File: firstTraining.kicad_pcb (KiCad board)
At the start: 2 copper layers, 147.3 x 50.8 mm, 17 parts, among them T1 Transformer_1P_SS, U1 TA48M05F, U2 TA48033S

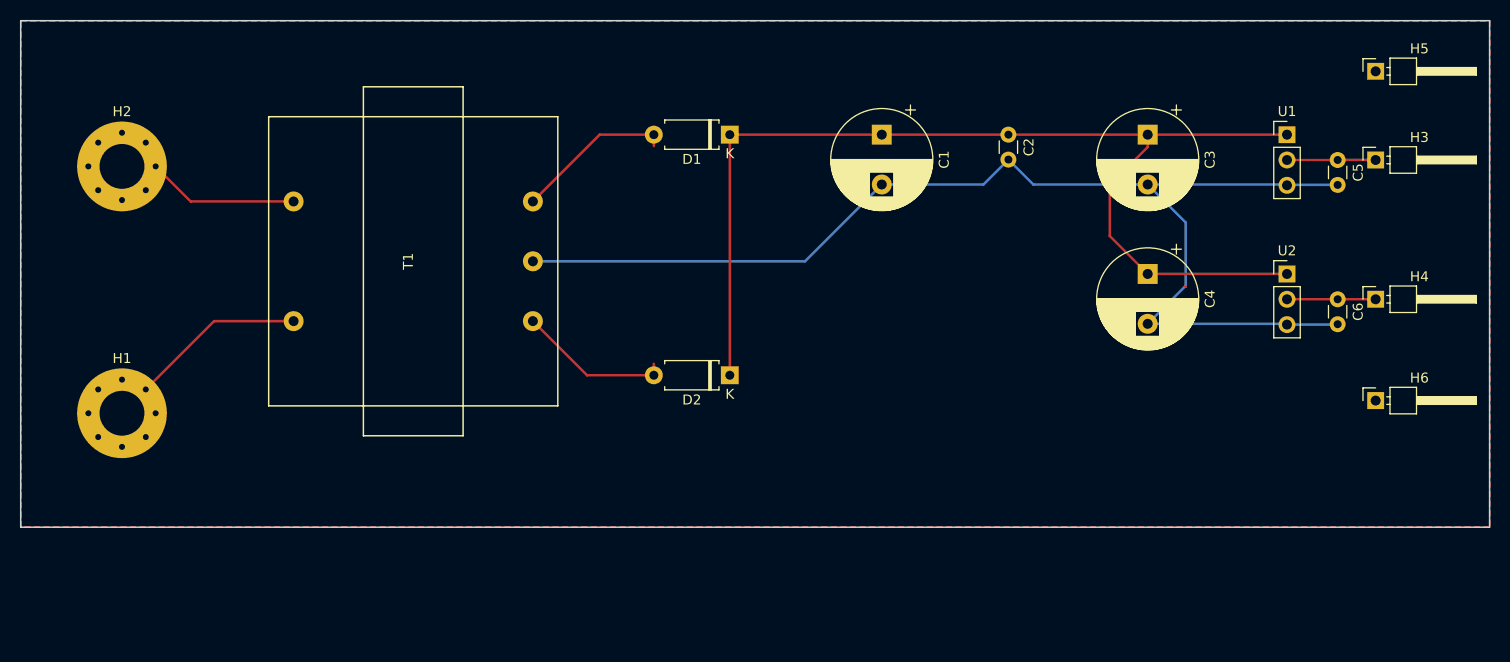
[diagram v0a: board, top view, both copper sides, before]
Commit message: Elecrowの最大寸法に入れた
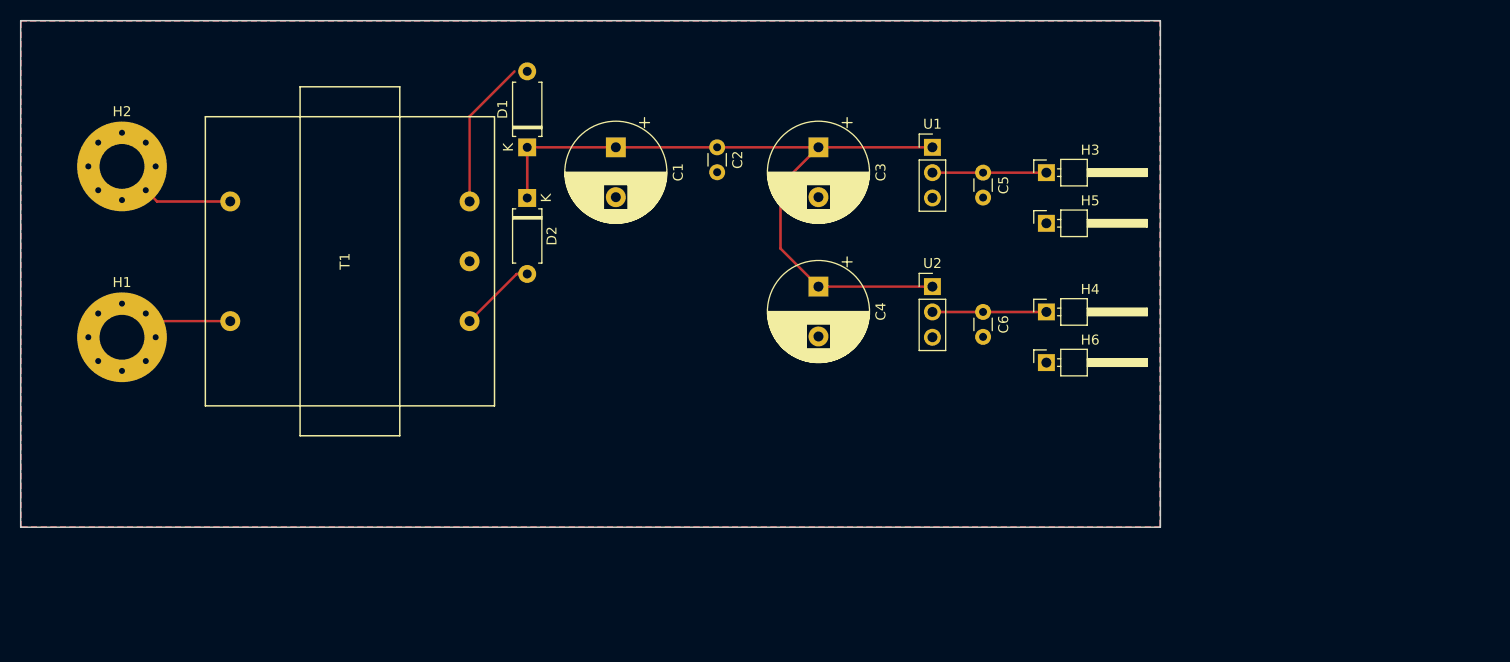
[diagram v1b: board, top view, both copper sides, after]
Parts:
- moved H5 36.4 mm to (166.4, 82.5)
- moved C5 35.6 mm to (160.0, 77.5)
- moved C6 35.6 mm to (160.0, 91.4)
- moved U1 35.6 mm to (154.9, 74.9)
- moved U2 35.6 mm to (154.9, 88.9)
- moved H6 33.2 mm to (166.4, 96.5)
- moved C3 33.0 mm to (143.5, 74.9)
- moved C4 33.0 mm to (143.5, 88.9)
- moved H3 33.0 mm to (166.4, 77.5)
- moved H4 33.0 mm to (166.4, 91.4)
- moved C2 29.2 mm to (133.3, 74.9)
- moved D2 27.0 mm to (114.3, 80.0), turned to 270 degrees
- moved C1 26.7 mm to (123.2, 74.9)
- moved D1 20.4 mm to (114.3, 74.9), turned to 90 degrees
- moved H1 7.62 mm to (73.7, 94.0)
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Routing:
- net GND: track 122.4 -> 0.00 mm
- net Net-(C1-Pad1): track 111.1 -> 74.3 mm
- net Net-(D2-Pad2): track 15.5 -> 7.74 mm
- net AC: track 17.7 -> 11.5 mm
- net Net-(C6-Pad1): track 8.89 -> 11.4 mm
- net Net-(C5-Pad1): track 8.89 -> 11.4 mm
- net Net-(H2-Pad1): track 15.3 -> 13.0 mm
- net Net-(D1-Pad2): track 16.1 -> 14.9 mm
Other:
- board size 147.3 x 50.8 mm -> 114.3 x 50.8 mm

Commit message: NETリスト更新, PCB図面新規作成
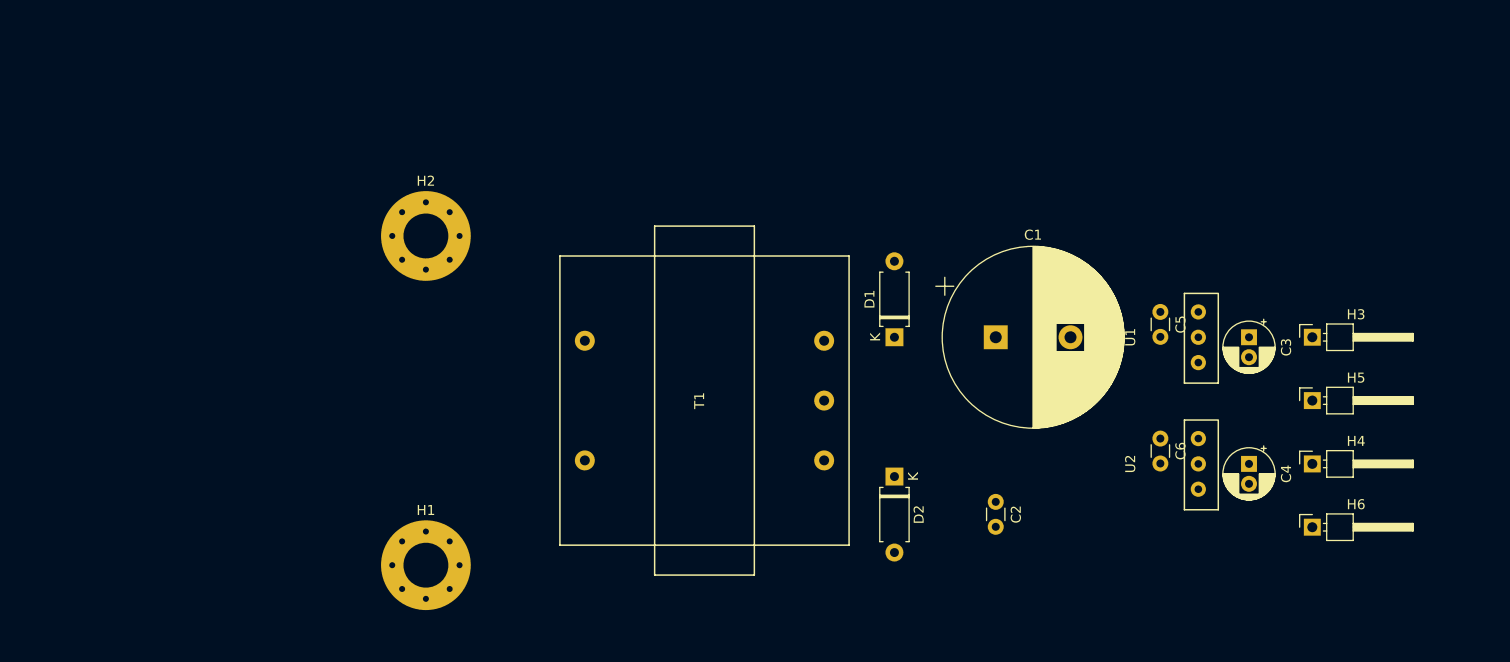
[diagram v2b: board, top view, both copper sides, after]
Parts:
- C1: footprint Capacitor_THT:CP_Radial_D10.0mm_P5.00mm -> Capacitor_THT:CP_Radial_D18.0mm_P7.50mm
- C3, C4: footprint Capacitor_THT:CP_Radial_D10.0mm_P5.00mm -> Capacitor_THT:CP_Radial_D5.0mm_P2.00mm
- U1, U2: footprint Connector_PinHeader_2.54mm:PinHeader_1x03_P2.54mm_Vertical -> newLib:TOSHIBA_DIP_Regulators
- moved C3 47.2 mm to (186.7, 94.0)
- moved C4 46.7 mm to (186.7, 106.7)
- moved D2 46.2 mm to (151.1, 108.0)
- moved C2 45.2 mm to (161.3, 110.5)
- moved C1 42.6 mm to (161.3, 94.0), turned to 0 degrees
- moved D1 41.5 mm to (151.1, 94.0)
- moved T1 38.2 mm to (132.1, 100.3)
- moved H1 38.1 mm to (104.1, 116.8)
- moved U1 32.8 mm to (181.6, 94.0), turned to 270 degrees
- moved U2 32.1 mm to (181.6, 106.7), turned to 270 degrees
- moved H5 32.1 mm to (193.0, 100.3)
- moved H3 31.4 mm to (193.0, 94.0)
- moved H6 31.4 mm to (193.0, 113.0)
- moved H2 31.3 mm to (104.1, 83.8)
- moved H4 30.7 mm to (193.0, 106.7)
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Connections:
- C3 pad 1: Net-(C1-Pad1) -> Net-(C3-Pad1)
- C4 pad 1: Net-(C1-Pad1) -> Net-(C4-Pad1)
- C5 pad 1: Net-(C5-Pad1) -> Net-(C1-Pad1)
- C6 pad 1: Net-(C6-Pad1) -> Net-(C1-Pad1)
- H3 pad 1: Net-(C5-Pad1) -> Net-(C3-Pad1)
- H4 pad 1: Net-(C6-Pad1) -> Net-(C4-Pad1)
- U1 pad 2: Net-(C5-Pad1) -> Net-(C3-Pad1)
- U2 pad 2: Net-(C6-Pad1) -> Net-(C4-Pad1)
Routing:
- net Net-(C1-Pad1): track 74.3 -> 0.00 mm
- net Net-(D1-Pad2): track 14.9 -> 0.00 mm
- net Net-(H2-Pad1): track 13.0 -> 0.00 mm
- net AC: track 11.5 -> 0.00 mm
- net Net-(C6-Pad1): track 11.4 -> 0.00 mm
- net Net-(C5-Pad1): track 11.4 -> 0.00 mm
- net Net-(D2-Pad2): track 7.74 -> 0.00 mm
- removed copper zone on B.Cu, net GND
- removed copper zone on F.Cu, net GND
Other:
- board outline removed
- net class Default: clearance 0.254 -> 0.2; trace_width 0.254 -> 0.25
- rule pad_to_mask_clearance: 0.051 -> 0
- rule trace_clearance: 0.254 -> 0.2
- rule via_min_drill: 0.4 -> 0.3
- rule via_min_size: 0.8 -> 0.4

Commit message: PCBを一部配線
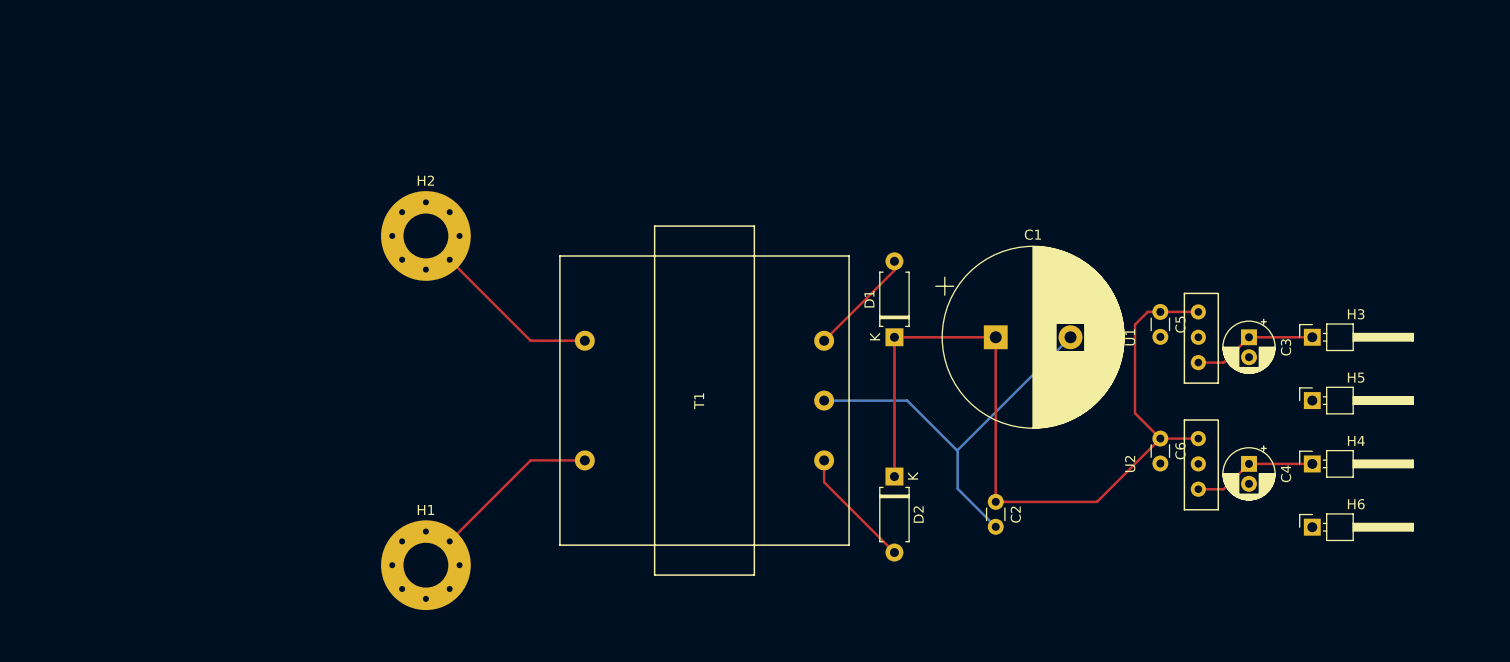
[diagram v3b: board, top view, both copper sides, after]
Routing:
- net Net-(C1-Pad1): track 0.00 -> 82.9 mm
- net GND: track 0.00 -> 40.8 mm
- net Net-(H2-Pad1): track 0.00 -> 20.3 mm
- net AC: track 0.00 -> 20.3 mm
- net Net-(C4-Pad1): track 0.00 -> 12.5 mm
- net Net-(C3-Pad1): track 0.00 -> 12.5 mm
- net Net-(D2-Pad2): track 0.00 -> 12.2 mm
- net Net-(D1-Pad2): track 0.00 -> 10.9 mm
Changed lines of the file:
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@@
     (thickness 1.6)
     (drawings 0)
-    (tracks 0)
+    (tracks 31)
     (zones 0)
     (modules 17)
@@
     (pad_drill 0.6)
     (pad_to_mask_clearance 0)
+    (solder_mask_min_width 0.25)
     (aux_axis_origin 0 0)
     (visible_elements FFFFFF7F)
@@
       (net 2 GND))
   )
+  (segment (start 151.13 93.98) (end 151.13 107.95) (width 0.25) (layer F.Cu) (net 1))
+  (segment (start 151.13 93.98) (end 161.29 93.98) (width 0.25) (layer F.Cu) (net 1))
+  (segment (start 161.29 93.98) (end 161.29 110.49) (width 0.25) (layer F.Cu) (net 1))
+  (segment (start 171.45 110.49) (end 177.8 104.14) (width 0.25) (layer F.Cu) (net 1))
+  (segment (start 161.29 110.49) (end 171.45 110.49) (width 0.25) (layer F.Cu) (net 1))
+  (segment (start 177.8 91.44) (end 176.53 91.44) (width 0.25) (layer F.Cu) (net 1))
+  (segment (start 176.53 91.44) (end 175.26 92.71) (width 0.25) (layer F.Cu) (net 1))
+  (segment (start 175.26 101.6) (end 177.8 104.14) (width 0.25) (layer F.Cu) (net 1))
+  (segment (start 175.26 92.71) (end 175.26 101.6) (width 0.25) (layer F.Cu) (net 1))
+  (segment (start 177.8 91.44) (end 181.61 91.44) (width 0.25) (layer F.Cu) (net 1))
+  (segment (start 177.8 104.14) (end 181.61 104.14) (width 0.25) (layer F.Cu) (net 1))
+  (segment (start 144.08 100.33) (end 152.4 100.33) (width 0.25) (layer B.Cu) (net 2))
+  (segment (start 152.4 100.33) (end 157.48 105.41) (width 0.25) (layer B.Cu) (net 2))
+  (segment (start 157.48 109.18) (end 161.29 112.99) (width 0.25) (layer B.Cu) (net 2))
+  (segment (start 157.48 105.41) (end 157.48 109.18) (width 0.25) (layer B.Cu) (net 2))
+  (segment (start 157.48 105.29) (end 168.79 93.98) (width 0.25) (layer B.Cu) (net 2))
+  (segment (start 157.48 105.41) (end 157.48 105.29) (width 0.25) (layer B.Cu) (net 2))
+  (segment (start 184.15 96.52) (end 186.69 93.98) (width 0.25) (layer F.Cu) (net 3))
+  (segment (start 181.61 96.52) (end 184.15 96.52) (width 0.25) (layer F.Cu) (net 3))
+  (segment (start 186.69 93.98) (end 193.04 93.98) (width 0.25) (layer F.Cu) (net 3))
+  (segment (start 184.15 109.22) (end 186.69 106.68) (width 0.25) (layer F.Cu) (net 4))
+  (segment (start 181.61 109.22) (end 184.15 109.22) (width 0.25) (layer F.Cu) (net 4))
+  (segment (start 186.69 106.68) (end 193.04 106.68) (width 0.25) (layer F.Cu) (net 4))
+  (segment (start 151.13 87.28) (end 151.13 86.36) (width 0.25) (layer F.Cu) (net 5))
+  (segment (start 144.08 94.33) (end 151.13 87.28) (width 0.25) (layer F.Cu) (net 5))
+  (segment (start 144.08 108.52) (end 151.13 115.57) (width 0.25) (layer F.Cu) (net 6))
+  (segment (start 144.08 106.33) (end 144.08 108.52) (width 0.25) (layer F.Cu) (net 6))
+  (segment (start 114.65 106.33) (end 104.14 116.84) (width 0.25) (layer F.Cu) (net 7))
+  (segment (start 120.08 106.33) (end 114.65 106.33) (width 0.25) (layer F.Cu) (net 7))
+  (segment (start 114.65 94.33) (end 104.14 83.82) (width 0.25) (layer F.Cu) (net 8))
+  (segment (start 120.08 94.33) (end 114.65 94.33) (width 0.25) (layer F.Cu) (net 8))
 )

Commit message: GNDベタを追加
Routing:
- added copper zone on B.Cu, net GND
- added copper zone on F.Cu, net GND
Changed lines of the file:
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@@
   (general
     (thickness 1.6)
-    (drawings 0)
+    (drawings 4)
     (tracks 31)
     (zones 0)
@@
       (net 2 GND))
   )
+  (gr_line (start 208.28 74.93) (end 91.44 74.93) (layer F.SilkS) (width 0.2))
+  (gr_line (start 208.28 124.46) (end 208.28 74.93) (layer F.SilkS) (width 0.2))
+  (gr_line (start 91.44 124.46) (end 208.28 124.46) (layer F.SilkS) (width 0.2))
+  (gr_line (start 91.44 74.93) (end 91.44 124.46) (layer F.SilkS) (width 0.2))
   (segment (start 151.13 93.98) (end 151.13 107.95) (width 0.25) (layer F.Cu) (net 1))
   (segment (start 151.13 93.98) (end 161.29 93.98) (width 0.25) (layer F.Cu) (net 1))
@@
   (segment (start 114.65 94.33) (end 104.14 83.82) (width 0.25) (layer F.Cu) (net 8))
   (segment (start 120.08 94.33) (end 114.65 94.33) (width 0.25) (layer F.Cu) (net 8))
+  (zone (net 2) (net_name GND) (layer F.Cu) (hatch edge 0.508)
+    (connect_pads (clearance 0.508))
+    (min_thickness 0.254)
+    (fill yes (arc_segments 16) (thermal_gap 0.508) (thermal_bridge_width 0.508))
+    (polygon
+      (pts
+        (xy 154.94 74.93) (xy 154.94 124.46) (xy 208.28 124.46) (xy 208.28 74.93)
+      )
+    )
+  )
+  (zone (net 2) (net_name GND) (layer B.Cu) (hatch edge 0.508)
+    (connect_pads (clearance 0.508))
+    (min_thickness 0.254)
+    (fill yes (arc_segments 16) (thermal_gap 0.508) (thermal_bridge_width 0.508))
+    (polygon
+      (pts
+        (xy 154.94 74.93) (xy 154.94 124.46) (xy 208.28 124.46) (xy 208.28 74.93)
+      )
+    )
+  )
 )
